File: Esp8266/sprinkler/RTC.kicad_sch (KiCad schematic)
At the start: 6 parts, among them U5 PCF8563T

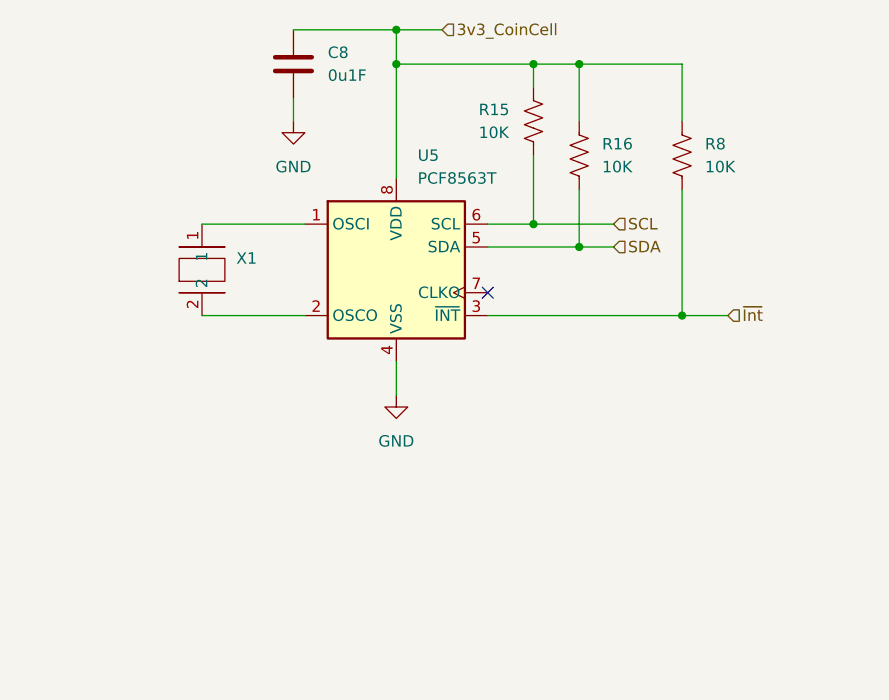
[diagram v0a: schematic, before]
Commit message: Transistor changes
Changed all Bjt transistors to Mosfets
Assign footprints
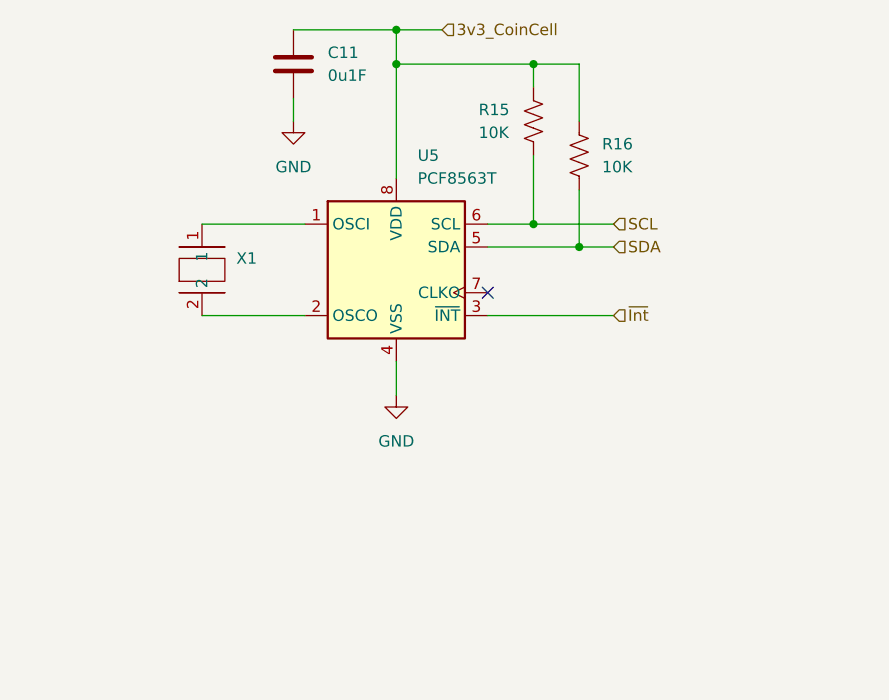
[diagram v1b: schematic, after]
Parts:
- removed R8: 10K, Resistor_SMD:R_0805_2012Metric_Pad1.20x1.40mm_HandSolder, symbol Device:R_US
- renumbered C8 to C11
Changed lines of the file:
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@@
 	(paper "A4")
-	(junction
-		(at 161.29 63.5)
-		(diameter 0)
-		(color 0 0 0 0)
-	)
 	(junction
 		(at 140.97 59.69)
@@
 	)
 	(junction
-		(at 172.72 91.44)
-		(diameter 0)
-		(color 0 0 0 0)
-	)
-	(junction
 		(at 156.21 63.5)
 		(diameter 0)
@@
 	(wire
 		(pts
-			(xy 172.72 63.5) (xy 161.29 63.5)
-		)
-		(stroke
-			(width 0)
-			(type default)
-		)
-	)
-	(wire
-		(pts
 			(xy 129.54 67.31) (xy 129.54 69.85)
 		)
@@
 	(wire
 		(pts
-			(xy 172.72 77.47) (xy 172.72 91.44)
-		)
-		(stroke
-			(width 0)
-			(type default)
-		)
-	)
-	(wire
-		(pts
 			(xy 140.97 76.2) (xy 140.97 63.5)
 		)
@@
 	(wire
 		(pts
-			(xy 151.13 91.44) (xy 172.72 91.44)
+			(xy 151.13 91.44) (xy 165.1 91.44)
 		)
 		(stroke
@@
 	(wire
 		(pts
-			(xy 172.72 91.44) (xy 177.8 91.44)
-		)
-		(stroke
-			(width 0)
-			(type default)
-		)
-	)
-	(wire
-		(pts
 			(xy 161.29 63.5) (xy 156.21 63.5)
 		)
@@
 		(pts
 			(xy 151.13 83.82) (xy 161.29 83.82)
-		)
-		(stroke
-			(width 0)
-			(type default)
-		)
-	)
-	(wire
-		(pts
-			(xy 172.72 69.85) (xy 172.72 63.5)
 		)
 		(stroke
@@
 	(hierarchical_label "~{Int}"
 		(shape input)
-		(at 177.8 91.44 0)
+		(at 165.1 91.44 0)
 		(effects
 			(font
@@
 		(dnp no)
 		(fields_autoplaced yes)
-		(property "Reference" "C8"
+		(property "Reference" "C11"
 			(at 133.35 62.23 0)
 			(effects
@@
 			(project ""
 				(path "/00ed8740-45a2-4b9d-9104-9548b81da339/c7a5ac99-aa8c-4314-b033-ede511422a71"
-					(reference "C8")
-					(unit 1)
-				)
-			)
-		)
-	)
-	(symbol
-		(lib_id "Device:R_US")
-		(at 172.72 73.66 0)
-		(unit 1)
-		(exclude_from_sim no)
-		(in_bom yes)
-		(on_board yes)
-		(dnp no)
-		(fields_autoplaced yes)
-		(property "Reference" "R8"
-			(at 175.26 72.39 0)
-			(effects
-				(font
-					(size 1.27 1.27)
-				)
-				(justify left)
-			)
-		)
-		(property "Value" "10K"
-			(at 175.26 74.93 0)
-			(effects
-				(font
-					(size 1.27 1.27)
-				)
-				(justify left)
-			)
-		)
-		(property "Footprint" "Resistor_SMD:R_0805_2012Metric_Pad1.20x1.40mm_HandSolder"
-			(at 173.736 73.914 90)
-			(effects
-				(font
-					(size 1.27 1.27)
-				)
-				(hide yes)
-			)
-		)
-		(property "Datasheet" "~"
-			(at 172.72 73.66 0)
-			(effects
-				(font
-					(size 1.27 1.27)
-				)
-				(hide yes)
-			)
-		)
-		(property "Description" "Resistor, US symbol"
-			(at 172.72 73.66 0)
-			(effects
-				(font
-					(size 1.27 1.27)
-				)
-				(hide yes)
-			)
-		)
-		(pin "2"
-		)
-		(pin "1"
-		)
-		(instances
-			(project "sprinkler"
-				(path "/00ed8740-45a2-4b9d-9104-9548b81da339/c7a5ac99-aa8c-4314-b033-ede511422a71"
-					(reference "R8")
+					(reference "C11")
 					(unit 1)
 				)
@@
 		(dnp no)
 		(fields_autoplaced yes)
-		(property "Reference" "#PWR023"
+		(property "Reference" "#PWR024"
 			(at 129.54 76.2 0)
 			(effects
@@
 			(project ""
 				(path "/00ed8740-45a2-4b9d-9104-9548b81da339/c7a5ac99-aa8c-4314-b033-ede511422a71"
-					(reference "#PWR023")
+					(reference "#PWR024")
 					(unit 1)
 				)
@@
 		(dnp no)
 		(fields_autoplaced yes)
-		(property "Reference" "#PWR022"
+		(property "Reference" "#PWR025"
 			(at 140.97 106.68 0)
 			(effects
@@
 			(project ""
 				(path "/00ed8740-45a2-4b9d-9104-9548b81da339/c7a5ac99-aa8c-4314-b033-ede511422a71"
-					(reference "#PWR022")
+					(reference "#PWR025")
 					(unit 1)
 				)

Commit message: Update connections
Connect Micro controller inputs and outputs
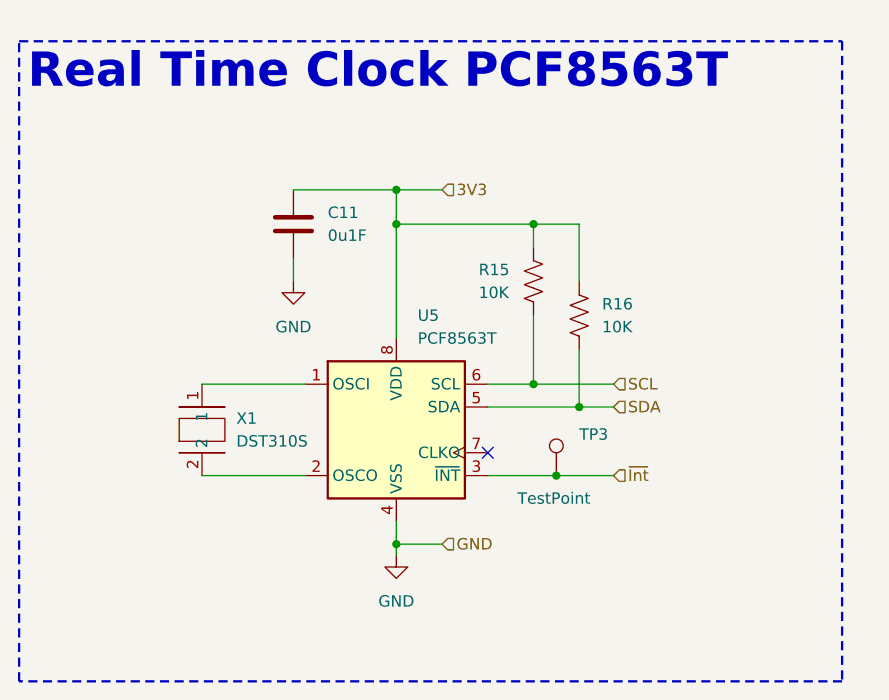
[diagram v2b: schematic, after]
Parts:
- added TP3: TestPoint, TestPoint:TestPoint_Pad_1.0x1.0mm, symbol Connector:TestPoint
- X1: value ~ -> DST310S
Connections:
- net ~{Int}: now also TP3.1
- net 3v3_CoinCell renamed 3V3
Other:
- moved on the sheet: C11, R15, R16, U5, X1

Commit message: pcb
First component layout (need to verify ESP8266 board size for fitment)
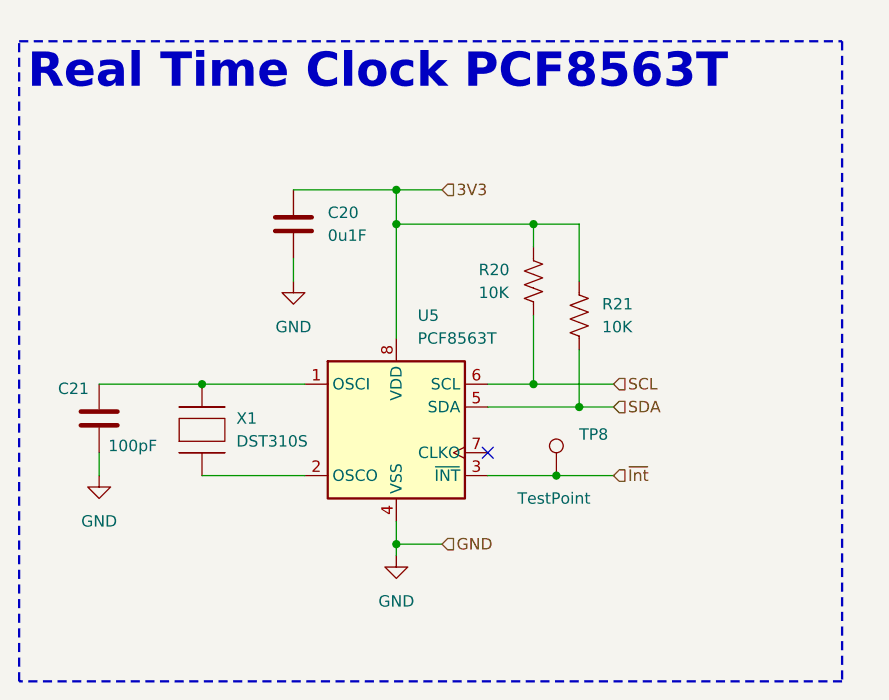
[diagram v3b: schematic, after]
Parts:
- added C21: 100pF, Capacitor_SMD:C_0805_2012Metric_Pad1.18x1.45mm_HandSolder, symbol Device:C
- renumbered C11 to C20, R15 to R20, R16 to R21, TP3 to TP8
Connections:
- net GND: now also C21.2
- net at U5.1 (OSCI), X1.1: now also C21.1
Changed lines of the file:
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@@
+	)
+	(junction
+		(at 119.38 99.06)
+		(diameter 0)
+		(color 0 0 0 0)
 	)
 	(junction
@@
 	(wire
 		(pts
+			(xy 107.95 99.06) (xy 119.38 99.06)
+		)
+		(stroke
+			(width 0)
+			(type default)
+		)
+	)
+	(wire
+		(pts
 			(xy 161.29 87.63) (xy 161.29 81.28)
 		)
@@
 		(pts
 			(xy 161.29 95.25) (xy 161.29 101.6)
+		)
+		(stroke
+			(width 0)
+			(type default)
+		)
+	)
+	(wire
+		(pts
+			(xy 107.95 106.68) (xy 107.95 109.22)
 		)
 		(stroke
@@
 		(dnp no)
 		(fields_autoplaced yes)
-		(property "Reference" "C11"
+		(property "Reference" "C20"
 			(at 133.35 80.01 0)
 			(effects
@@
 			(project ""
 				(path "/00ed8740-45a2-4b9d-9104-9548b81da339/c7a5ac99-aa8c-4314-b033-ede511422a71"
-					(reference "C11")
+					(reference "C20")
 					(unit 1)
 				)
@@
 		(on_board yes)
 		(dnp no)
-		(property "Reference" "TP3"
+		(property "Reference" "TP8"
 			(at 161.29 104.648 0)
 			(effects
@@
 			(project "sprinkler"
 				(path "/00ed8740-45a2-4b9d-9104-9548b81da339/c7a5ac99-aa8c-4314-b033-ede511422a71"
-					(reference "TP3")
+					(reference "TP8")
+					(unit 1)
+				)
+			)
+		)
+	)
+	(symbol
+		(lib_id "Device:C")
+		(at 107.95 102.87 0)
+		(unit 1)
+		(exclude_from_sim no)
+		(in_bom yes)
+		(on_board yes)
+		(dnp no)
+		(property "Reference" "C21"
+			(at 103.378 99.568 0)
+			(effects
+				(font
+					(size 1.27 1.27)
+				)
+				(justify left)
+			)
+		)
+		(property "Value" "100pF"
+			(at 108.966 105.918 0)
+			(effects
+				(font
+					(size 1.27 1.27)
+				)
+				(justify left)
+			)
+		)
+		(property "Footprint" "Capacitor_SMD:C_0805_2012Metric_Pad1.18x1.45mm_HandSolder"
+			(at 108.9152 106.68 0)
+			(effects
+				(font
+					(size 1.27 1.27)
+				)
+				(hide yes)
+			)
+		)
+		(property "Datasheet" "~"
+			(at 107.95 102.87 0)
+			(effects
+				(font
+					(size 1.27 1.27)
+				)
+				(hide yes)
+			)
+		)
+		(property "Description" "Unpolarized capacitor"
+			(at 107.95 102.87 0)
+			(effects
+				(font
+					(size 1.27 1.27)
+				)
+				(hide yes)
+			)
+		)
+		(pin "1"
+		)
+		(pin "2"
+		)
+		(instances
+			(project ""
+				(path "/00ed8740-45a2-4b9d-9104-9548b81da339/c7a5ac99-aa8c-4314-b033-ede511422a71"
+					(reference "C21")
 					(unit 1)
 				)
@@
 		(dnp no)
 		(fields_autoplaced yes)
-		(property "Reference" "#PWR024"
+		(property "Reference" "#PWR033"
 			(at 129.54 93.98 0)
 			(effects
@@
 			(project ""
 				(path "/00ed8740-45a2-4b9d-9104-9548b81da339/c7a5ac99-aa8c-4314-b033-ede511422a71"
-					(reference "#PWR024")
+					(reference "#PWR033")
 					(unit 1)
 				)
@@
 		(dnp no)
 		(fields_autoplaced yes)
-		(property "Reference" "#PWR025"
+		(property "Reference" "#PWR034"
 			(at 140.97 124.46 0)
 			(effects
@@
 			(project ""
 				(path "/00ed8740-45a2-4b9d-9104-9548b81da339/c7a5ac99-aa8c-4314-b033-ede511422a71"
-					(reference "#PWR025")
+					(reference "#PWR034")
+					(unit 1)
+				)
+			)
+		)
+	)
+	(symbol
+		(lib_id "power:GND")
+		(at 107.95 109.22 0)
+		(unit 1)
+		(exclude_from_sim no)
+		(in_bom yes)
+		(on_board yes)
+		(dnp no)
+		(fields_autoplaced yes)
+		(property "Reference" "#PWR038"
+			(at 107.95 115.57 0)
+			(effects
+				(font
+					(size 1.27 1.27)
+				)
+				(hide yes)
+			)
+		)
+		(property "Value" "GND"
+			(at 107.95 114.3 0)
+			(effects
+				(font
+					(size 1.27 1.27)
+				)
+			)
+		)
+		(property "Footprint" ""
+			(at 107.95 109.22 0)
+			(effects
+				(font
+					(size 1.27 1.27)
+				)
+				(hide yes)
+			)
+		)
+		(property "Datasheet" ""
+			(at 107.95 109.22 0)
+			(effects
+				(font
+					(size 1.27 1.27)
+				)
+				(hide yes)
+			)
+		)
+		(property "Description" "Power symbol creates a global label with name \"GND\" , ground"
+			(at 107.95 109.22 0)
+			(effects
+				(font
+					(size 1.27 1.27)
+				)
+				(hide yes)
+			)
+		)
+		(pin "1"
+		)
+		(instances
+			(project "sprinkler"
+				(path "/00ed8740-45a2-4b9d-9104-9548b81da339/c7a5ac99-aa8c-4314-b033-ede511422a71"
+					(reference "#PWR038")
 					(unit 1)
 				)
@@
 		(dnp no)
 		(fields_autoplaced yes)
-		(property "Reference" "R16"
+		(property "Reference" "R21"
 			(at 163.83 90.17 0)
 			(effects
@@
 			(project ""
 				(path "/00ed8740-45a2-4b9d-9104-9548b81da339/c7a5ac99-aa8c-4314-b033-ede511422a71"
-					(reference "R16")
+					(reference "R21")
 					(unit 1)
 				)
@@
 		(on_board yes)
 		(dnp no)
-		(property "Reference" "R15"
+		(property "Reference" "R20"
 			(at 150.114 86.36 0)
 			(effects
@@
 			(project ""
 				(path "/00ed8740-45a2-4b9d-9104-9548b81da339/c7a5ac99-aa8c-4314-b033-ede511422a71"
-					(reference "R15")
+					(reference "R20")
 					(unit 1)
 				)
